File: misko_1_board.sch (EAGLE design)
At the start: 147 parts, among them IC1 ATMEGA1281-16AU, IC10 ORG1510-MK4, IC11 TPS3808G33DBVT, IC12 LTC4425, IC13 RN4678_BT_MODULE, IC14 ADXL345, IC15 74HCT1G32, IC16 FM25W256-SOIC, IC17 MICROSD_SPI_MODE, IC18 FH12-30S-0.5SH, IC19 DS1394U-33+, IC2 MC1525TT, IC20 ATWINC1500-MR210PB, IC21 115Q-BCA0, IC22 SIM800, IC3 TMP36GRTZ, IC4 TPS63031, IC5 MCP73871-2AAI/ML, IC6 MAX6818, IC7 FT230XS, IC8 SN74LVC1G3157DBVR - BT switch, IC9 SN74LVC1G3157DBVR - GPS switch, Q1 ABM3B, Q2 LFXTAL016178R, SW1 RESET, SW2 POWER SWITCH, SW3 MICROJOYSTICK, SW4 PB6156RSL, SW5 PB6156RSL, T1 BSS84

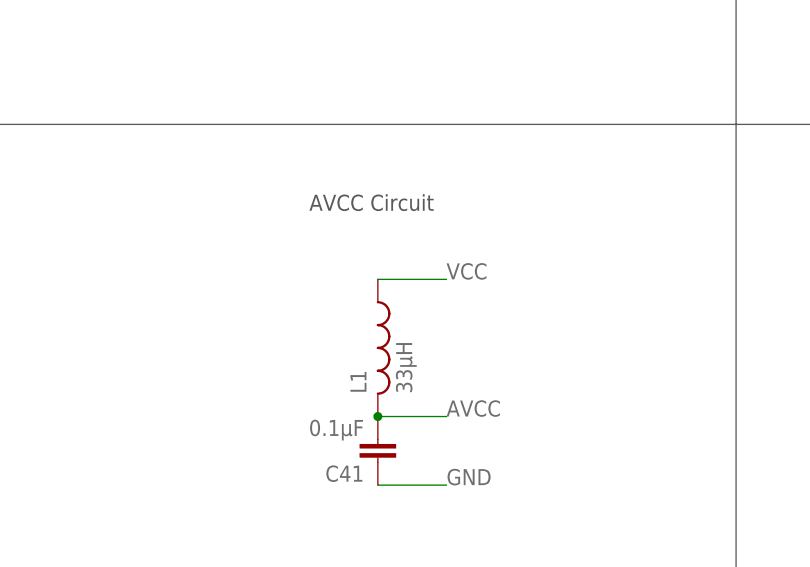
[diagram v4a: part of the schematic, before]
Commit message: - corrected values for L1
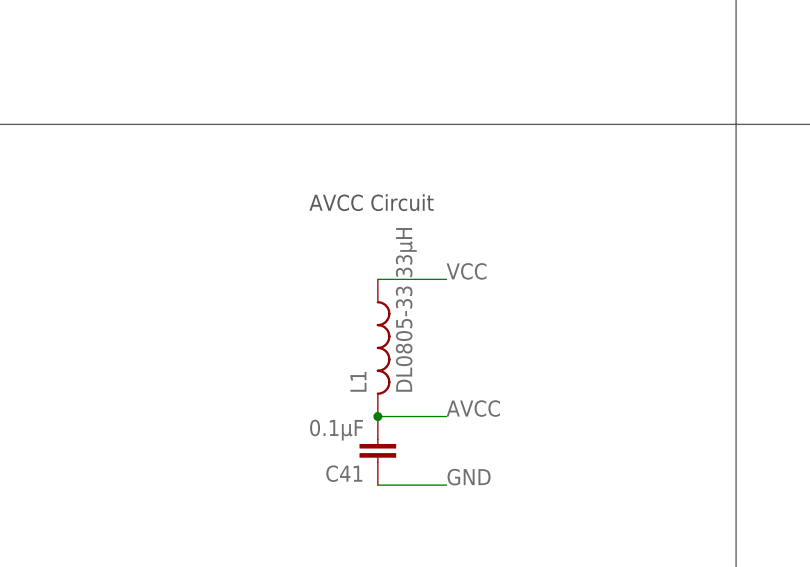
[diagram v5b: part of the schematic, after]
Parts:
- L1: value 33µH -> DL0805-33 33µH
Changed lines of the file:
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@@
 <?xml version="1.0" encoding="utf-8"?>
 <!DOCTYPE eagle SYSTEM "eagle.dtd">
-<eagle version="8.2.2">
+<eagle version="8.3.1">
 <drawing>
 <settings>
 <setting alwaysvectorfont="no"/>
+<setting keepoldvectorfont="yes"/>
 <setting verticaltext="up"/>
 </settings>
-<grid distance="0.1" unitdist="inch" unit="mm" style="lines" multiple="1" display="no" altdistance="0.01" altunitdist="mm" altunit="mm"/>
+<grid distance="0.1" unitdist="inch" unit="inch" style="lines" multiple="1" display="no" altdistance="0.01" altunitdist="inch" altunit="inch"/>
 <layers>
-<layer number="1" name="Top" color="4" fill="1" visible="yes" active="no"/>
-<layer number="2" name="Route2" color="1" fill="3" visible="yes" active="no"/>
-<layer number="3" name="Route3" color="4" fill="3" visible="yes" active="no"/>
-<layer number="4" name="Route4" color="1" fill="4" visible="yes" active="no"/>
-<layer number="5" name="Route5" color="4" fill="4" visible="yes" active="no"/>
-<layer number="6" name="Route6" color="1" fill="8" visible="yes" active="no"/>
-<layer number="7" name="Route7" color="4" fill="8" visible="yes" active="no"/>
-<layer number="8" name="Route8" color="1" fill="2" visible="yes" active="no"/>
-<layer number="9" name="Route9" color="4" fill="2" visible="yes" active="no"/>
-<layer number="10" name="Route10" color="1" fill="7" visible="yes" active="no"/>
-<layer number="11" name="Route11" color="4" fill="7" visible="yes" active="no"/>
-<layer number="12" name="Route12" color="1" fill="5" visible="yes" active="no"/>
-<layer number="13" name="Route13" color="4" fill="5" visible="yes" active="no"/>
-<layer number="14" name="Route14" color="1" fill="6" visible="yes" active="no"/>
-<layer number="15" name="Route15" color="4" fill="6" visible="yes" active="no"/>
-<layer number="16" name="Bottom" color="1" fill="1" visible="yes" active="no"/>
-<layer number="17" name="Pads" color="2" fill="1" visible="yes" active="no"/>
-<layer number="18" name="Vias" color="2" fill="1" visible="yes" active="no"/>
-<layer number="19" name="Unrouted" color="6" fill="1" visible="yes" active="no"/>
-<layer number="20" name="Dimension" color="15" fill="1" visible="yes" active="no"/>
-<layer number="21" name="tPlace" color="7" fill="1" visible="yes" active="no"/>
-<layer number="22" name="bPlace" color="7" fill="1" visible="yes" active="no"/>
-<layer number="23" name="tOrigins" color="15" fill="1" visible="yes" active="no"/>
-<layer number="24" name="bOrigins" color="15" fill="1" visible="yes" active="no"/>
-<layer number="25" name="tNames" color="7" fill="1" visible="yes" active="no"/>
-<layer number="26" name="bNames" color="7" fill="1" visible="yes" active="no"/>
-<layer number="27" name="tValues" color="7" fill="1" visible="yes" active="no"/>
-<layer number="28" name="bValues" color="7" fill="1" visible="yes" active="no"/>
+<layer number="1" name="Top" color="4" fill="1" visible="no" active="no"/>
+<layer number="2" name="Route2" color="1" fill="3" visible="no" active="no"/>
+<layer number="3" name="Route3" color="4" fill="3" visible="no" active="no"/>
+<layer number="4" name="Route4" color="1" fill="4" visible="no" active="no"/>
+<layer number="5" name="Route5" color="4" fill="4" visible="no" active="no"/>
+<layer number="6" name="Route6" color="1" fill="8" visible="no" active="no"/>
+<layer number="7" name="Route7" color="4" fill="8" visible="no" active="no"/>
+<layer number="8" name="Route8" color="1" fill="2" visible="no" active="no"/>
+<layer number="9" name="Route9" color="4" fill="2" visible="no" active="no"/>
+<layer number="10" name="Route10" color="1" fill="7" visible="no" active="no"/>
+<layer number="11" name="Route11" color="4" fill="7" visible="no" active="no"/>
+<layer number="12" name="Route12" color="1" fill="5" visible="no" active="no"/>
+<layer number="13" name="Route13" color="4" fill="5" visible="no" active="no"/>
+<layer number="14" name="Route14" color="1" fill="6" visible="no" active="no"/>
+<layer number="15" name="Route15" color="4" fill="6" visible="no" active="no"/>
+<layer number="16" name="Bottom" color="1" fill="1" visible="no" active="no"/>
+<layer number="17" name="Pads" color="2" fill="1" visible="no" active="no"/>
+<layer number="18" name="Vias" color="2" fill="1" visible="no" active="no"/>
+<layer number="19" name="Unrouted" color="6" fill="1" visible="no" active="no"/>
+<layer number="20" name="Dimension" color="15" fill="1" visible="no" active="no"/>
+<layer number="21" name="tPlace" color="7" fill="1" visible="no" active="no"/>
+<layer number="22" name="bPlace" color="7" fill="1" visible="no" active="no"/>
+<layer number="23" name="tOrigins" color="15" fill="1" visible="no" active="no"/>
+<layer number="24" name="bOrigins" color="15" fill="1" visible="no" active="no"/>
+<layer number="25" name="tNames" color="7" fill="1" visible="no" active="no"/>
+<layer number="26" name="bNames" color="7" fill="1" visible="no" active="no"/>
+<layer number="27" name="tValues" color="7" fill="1" visible="no" active="no"/>
+<layer number="28" name="bValues" color="7" fill="1" visible="no" active="no"/>
 <layer number="29" name="tStop" color="7" fill="3" visible="no" active="no"/>
 <layer number="30" name="bStop" color="7" fill="6" visible="no" active="no"/>
@@
 <layer number="35" name="tGlue" color="7" fill="4" visible="no" active="no"/>
 <layer number="36" name="bGlue" color="7" fill="5" visible="no" active="no"/>
-<layer number="37" name="tTest" color="7" fill="1" visible="yes" active="no"/>
-<layer number="38" name="bTest" color="7" fill="1" visible="yes" active="no"/>
+<layer number="37" name="tTest" color="7" fill="1" visible="no" active="no"/>
+<layer number="38" name="bTest" color="7" fill="1" visible="no" active="no"/>
 <layer number="39" name="tKeepout" color="4" fill="11" visible="no" active="no"/>
 <layer number="40" name="bKeepout" color="1" fill="11" visible="no" active="no"/>
@@
 <layer number="44" name="Drills" color="7" fill="1" visible="no" active="no"/>
 <layer number="45" name="Holes" color="7" fill="1" visible="no" active="no"/>
-<layer number="46" name="Milling" color="3" fill="1" visible="yes" active="no"/>
-<layer number="47" name="Measures" color="7" fill="1" visible="yes" active="no"/>
-<layer number="48" name="Document" color="7" fill="1" visible="yes" active="no"/>
-<layer number="49" name="Reference" color="7" fill="1" visible="yes" active="no"/>
-<layer number="50" name="dxf" color="7" fill="1" visible="yes" active="no"/>
-<layer number="51" name="tDocu" color="7" fill="1" visible="yes" active="no"/>
-<layer number="52" name="bDocu" color="7" fill="1" visible="yes" active="no"/>
-<layer number="53" name="tGND_GNDA" color="7" fill="9" visible="yes" active="no"/>
-<layer number="54" name="bGND_GNDA" color="1" fill="9" visible="yes" active="no"/>
-<layer number="56" name="wert" color="7" fill="1" visible="yes" active="no"/>
-<layer number="57" name="tCAD" color="7" fill="1" visible="yes" active="no"/>
-<layer number="59" name="tCarbon" color="7" fill="1" visible="yes" active="no"/>
-<layer number="60" name="bCarbon" color="7" fill="1" visible="yes" active="no"/>
+<layer number="46" name="Milling" color="3" fill="1" visible="no" active="no"/>
+<layer number="47" name="Measures" color="7" fill="1" visible="no" active="no"/>
+<layer number="48" name="Document" color="7" fill="1" visible="no" active="no"/>
+<layer number="49" name="Reference" color="7" fill="1" visible="no" active="no"/>
+<layer number="50" name="dxf" color="7" fill="1" visible="no" active="no"/>
+<layer number="51" name="tDocu" color="7" fill="1" visible="no" active="no"/>
+<layer number="52" name="bDocu" color="7" fill="1" visible="no" active="no"/>
+<layer number="53" name="tGND_GNDA" color="7" fill="9" visible="no" active="no"/>
+<layer number="54" name="bGND_GNDA" color="1" fill="9" visible="no" active="no"/>
+<layer number="56" name="wert" color="7" fill="1" visible="no" active="no"/>
+<layer number="57" name="tCAD" color="7" fill="1" visible="no" active="no"/>
+<layer number="59" name="tCarbon" color="7" fill="1" visible="no" active="no"/>
+<layer number="60" name="bCarbon" color="7" fill="1" visible="no" active="no"/>
 <layer number="90" name="Modules" color="5" fill="1" visible="yes" active="yes"/>
 <layer number="91" name="Nets" color="2" fill="1" visible="yes" active="yes"/>
@@
 <part name="C22" library="rcl" deviceset="C-EU" device="C0805" value="10µF"/>
 <part name="C41" library="resistor" library_urn="urn:adsk.eagle:library:348" deviceset="C-EU" device="C0805" value="0.1µF"/>
-<part name="L1" library="rcl" deviceset="L-US" device="" value="33µH"/>
+<part name="L1" library="rcl" deviceset="L-US" device="" value="DL0805-33 33µH"/>
 <part name="CONN5" library="discrete" deviceset="ANTENNA" device="SMD" value="U.FL-R-SMT 1"/>
 <part name="IC17" library="Molex SD-47309 SD Card Slot" deviceset="MICROSD_SPI_MODE" device=""/>
@@
 <compatibility>
 <note version="8.2" severity="warning">
-Since Version 8.2, Eagle supports online libraries. The ids
+Since Version 8.2, EAGLE supports online libraries. The ids
 of those online libraries will not be understood (or retained)
 with this version.

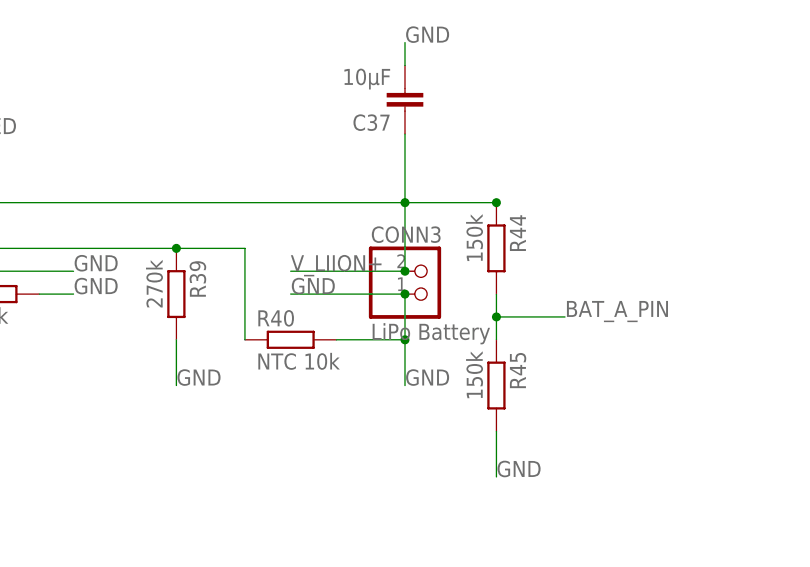
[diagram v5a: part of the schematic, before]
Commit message: - rotated JST-PH connector so that it is placed in accordance with the battery polarity on its JST connector (was reversed before the change)
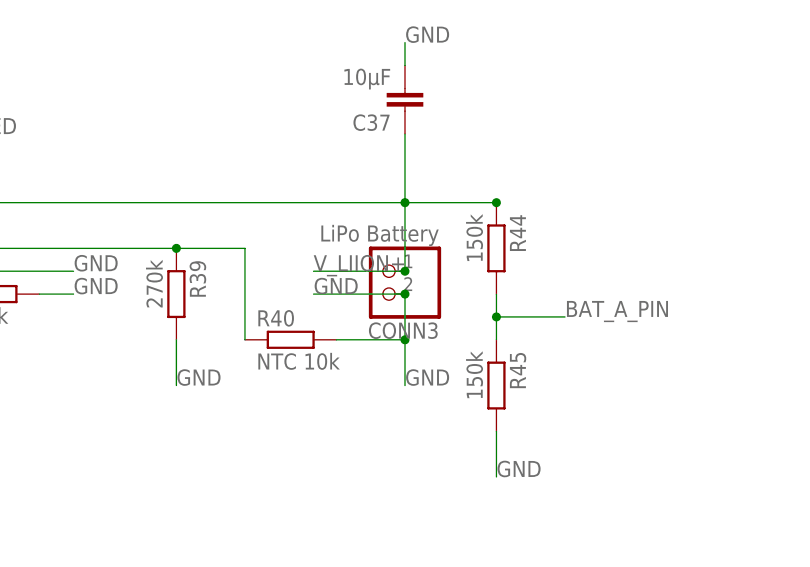
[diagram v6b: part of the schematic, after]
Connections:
- net GND: now also CONN3.1; no longer CONN3.2
- net V_LIION+: now also CONN3.2; no longer CONN3.1
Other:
- moved on the sheet: CONN3
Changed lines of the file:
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@@
 <instance part="SW2" gate="G$1" x="40.64" y="467.36" rot="R90"/>
 <instance part="C20" gate="G$1" x="182.88" y="596.9" rot="R180"/>
-<instance part="CONN3" gate="G$1" x="320.04" y="510.54"/>
+<instance part="CONN3" gate="G$1" x="314.96" y="513.08" rot="R180"/>
 <instance part="C2" gate="G$1" x="24.13" y="43.18"/>
 <instance part="C7" gate="G$1" x="78.74" y="66.04"/>
@@
 <pinref part="R40" gate="G$1" pin="2"/>
 <wire x1="309.88" y1="505.46" x2="317.5" y2="505.46" width="0.1524" layer="91"/>
-<pinref part="CONN3" gate="G$1" pin="2"/>
+<label x="317.5" y="500.38" size="1.778" layer="95" ratio="9"/>
+<pinref part="CONN3" gate="G$1" pin="1"/>
 <wire x1="317.5" y1="510.54" x2="317.5" y2="505.46" width="0.1524" layer="91"/>
 <junction x="317.5" y="505.46"/>
-<wire x1="317.5" y1="510.54" x2="304.8" y2="510.54" width="0.1524" layer="91"/>
+<wire x1="317.5" y1="510.54" x2="307.34" y2="510.54" width="0.1524" layer="91"/>
 <junction x="317.5" y="510.54"/>
-<label x="304.8" y="510.54" size="1.778" layer="95"/>
-<label x="317.5" y="500.38" size="1.778" layer="95" ratio="9"/>
+<label x="307.34" y="510.54" size="1.778" layer="95"/>
 </segment>
 <segment>
@@
 <wire x1="317.5" y1="528.32" x2="317.5" y2="520.7" width="0.1524" layer="91"/>
 <junction x="327.66" y="520.7"/>
-<pinref part="CONN3" gate="G$1" pin="1"/>
-<wire x1="317.5" y1="513.08" x2="317.5" y2="520.7" width="0.1524" layer="91"/>
-<wire x1="317.5" y1="513.08" x2="304.8" y2="513.08" width="0.1524" layer="91"/>
-<junction x="317.5" y="513.08"/>
-<label x="304.8" y="513.08" size="1.778" layer="95"/>
 <pinref part="IC5" gate="A" pin="VBAT_SENSE"/>
 <pinref part="IC5" gate="A" pin="VBAT2"/>
 <pinref part="IC5" gate="A" pin="VBAT1"/>
-</segment>
-<segment>
+<pinref part="CONN3" gate="G$1" pin="2"/>
+<wire x1="317.5" y1="513.08" x2="307.34" y2="513.08" width="0.1524" layer="91"/>
+<wire x1="317.5" y1="513.08" x2="317.5" y2="520.7" width="0.1524" layer="91"/>
+<junction x="317.5" y="513.08"/>
+<label x="307.34" y="513.08" size="1.778" layer="95"/>
+</segment>
+<segment>

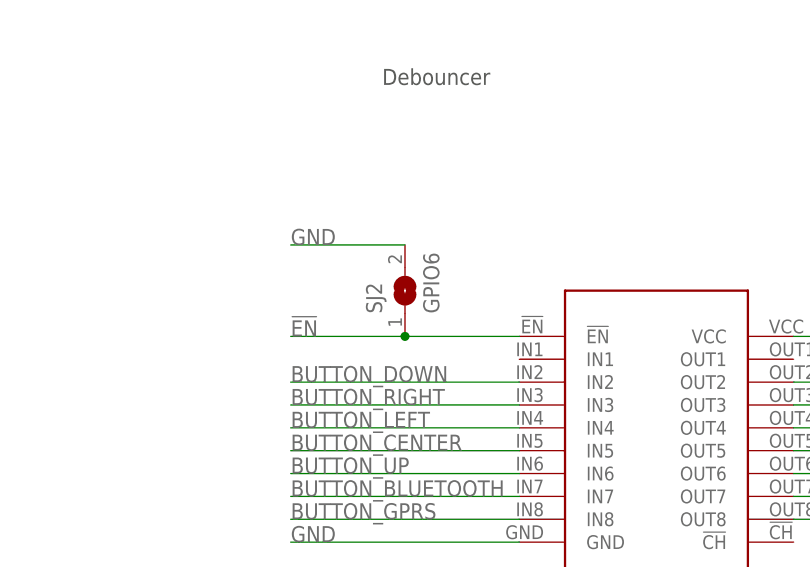
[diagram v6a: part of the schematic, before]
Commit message: - grounded MAX6818 !EN! pin to work properly: now key release is high, key press is low on the joystick and buttons
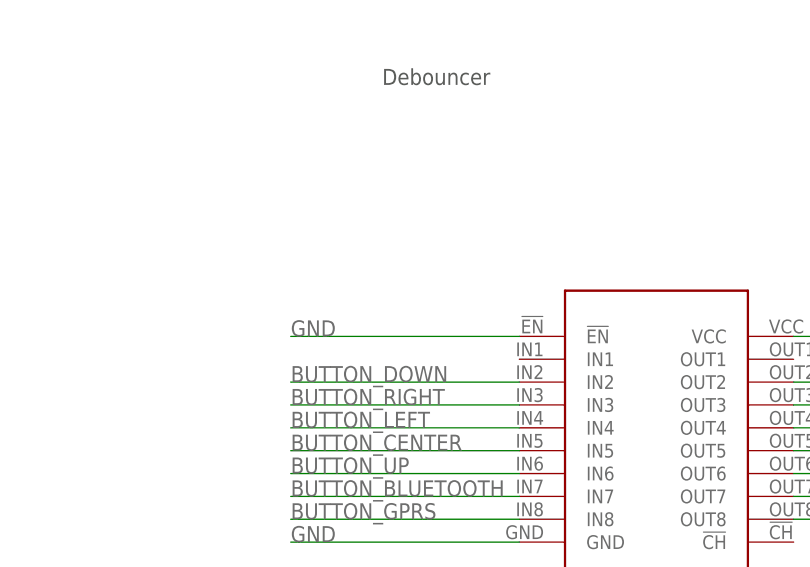
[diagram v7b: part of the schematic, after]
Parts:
- removed SJ2: GPIO6, jumper:SJW
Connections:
- removed net !EN!: IC6.!EN!, SJ2.1
- net GND: now also IC6.!EN!; no longer SJ2.2
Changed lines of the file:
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@@
 <part name="IC6" library="MAX6818 CMOS Switch debouncer" deviceset="MAX6818" device=""/>
 <part name="C34" library="rcl" deviceset="C-EU" device="C0805" value="10µF"/>
-<part name="SJ2" library="jumper" deviceset="SJ" device="W" value="GPIO6"/>
 <part name="IC13" library="RN4678 Bluetooth 4.2 Dual Mode" deviceset="RN4678_BT_MODULE" device=""/>
 <part name="R43" library="resistor" library_urn="urn:adsk.eagle:library:348" deviceset="R-EU_" device="R0805" value="10k"/>
@@
 <instance part="IC6" gate="G$1" x="281.94" y="353.06"/>
 <instance part="C34" gate="G$1" x="307.34" y="368.3" rot="R180"/>
-<instance part="SJ2" gate="1" x="254" y="370.84" rot="R90"/>
 <instance part="IC13" gate="G$1" x="119.38" y="-25.4"/>
 <instance part="R43" gate="G$1" x="218.44" y="-38.1"/>
@@
 </segment>
 <segment>
-<wire x1="254" y1="375.92" x2="241.3" y2="375.92" width="0.1524" layer="91"/>
-<label x="241.3" y="375.92" size="1.778" layer="95"/>
-<pinref part="SJ2" gate="1" pin="2"/>
-</segment>
-<segment>
 <pinref part="IC13" gate="G$1" pin="GND"/>
 <wire x1="134.62" y1="-12.7" x2="142.24" y2="-12.7" width="0.1524" layer="91"/>
@@
 <label x="165.1" y="-40.64" size="1.778" layer="95"/>
 </segment>
+<segment>
+<pinref part="IC6" gate="G$1" pin="!EN!"/>
+<wire x1="266.7" y1="365.76" x2="241.3" y2="365.76" width="0.1524" layer="91"/>
+<label x="241.3" y="365.76" size="1.778" layer="95"/>
+</segment>
 </net>
 <net name="5V0" class="1">
@@
 </segment>
 </net>
-<net name="!EN!" class="2">
-<segment>
-<pinref part="IC6" gate="G$1" pin="!EN!"/>
-<label x="241.3" y="365.76" size="1.778" layer="95"/>
-<wire x1="266.7" y1="365.76" x2="254" y2="365.76" width="0.1524" layer="91"/>
-<pinref part="SJ2" gate="1" pin="1"/>
-<wire x1="254" y1="365.76" x2="241.3" y2="365.76" width="0.1524" layer="91"/>
-<junction x="254" y="365.76"/>
-</segment>
-</net>
